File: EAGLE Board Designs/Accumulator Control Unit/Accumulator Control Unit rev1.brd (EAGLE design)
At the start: 186.7 x 135.7 mm, 223 parts, among them J1 CONNECTOR-CAN_MF_T_V_, J2 CONNECTOR-8_MF_T_V_, J3 CONNECTOR-8_MF_T_V_, J4 CONNECTOR-2_MF_T_V_, J5 CONNECTOR-12_MF_T_V_, J6 CONNECTOR-14_MF_T_V_, Q1 TRANSISTOR_N_MOS__PMV15ENEA, Q2 TRANSISTOR_N_MOS__PMV15ENEA, T1 TRANSFORMER_HM2112ZNLT_AIRGAP, U1 RELAY_SOLIDSTATE_NO, U10 OPAMP_1_CHANNEL_OPA991, U11 LOGICGATE_AND_DCK3, U12 OPAMP_1_CHANNEL_OPA991, U13 OPAMP_1_CHANNEL_OPA991, U14 OPAMP_1_CHANNEL_OPA991, U15 LOGICGATE_AND_DCK3, U16 RELAY_SOLIDSTATE_NO, U17 VOLTAGE_REGULATOR_SOT223_3.3V, U18 OPAMP_1_CHANNEL_OPA991, U19 MAX7404, U2 ADG1423, U20 OPAMP_1_CHANNEL_OPA991, U22 OPAMP_1_CHANNEL_OPA991, U25 TCAN1051HQV-Q1, U26 MAX7404, U27 OPAMP_1_CHANNEL_OPA991, U28 MAX7404, U29 OPAMP_1_CHANNEL_OPA991, U3 LM555, U30 MAX7404, U4 OPAMP_1_CHANNEL_OPA991, U5 LTC6820, U6 ADM823, U7 OPAMP_1_CHANNEL_OPA991, U8 LOGICGATE_AND_DCK3, U9 OPAMP_1_CHANNEL_OPA991

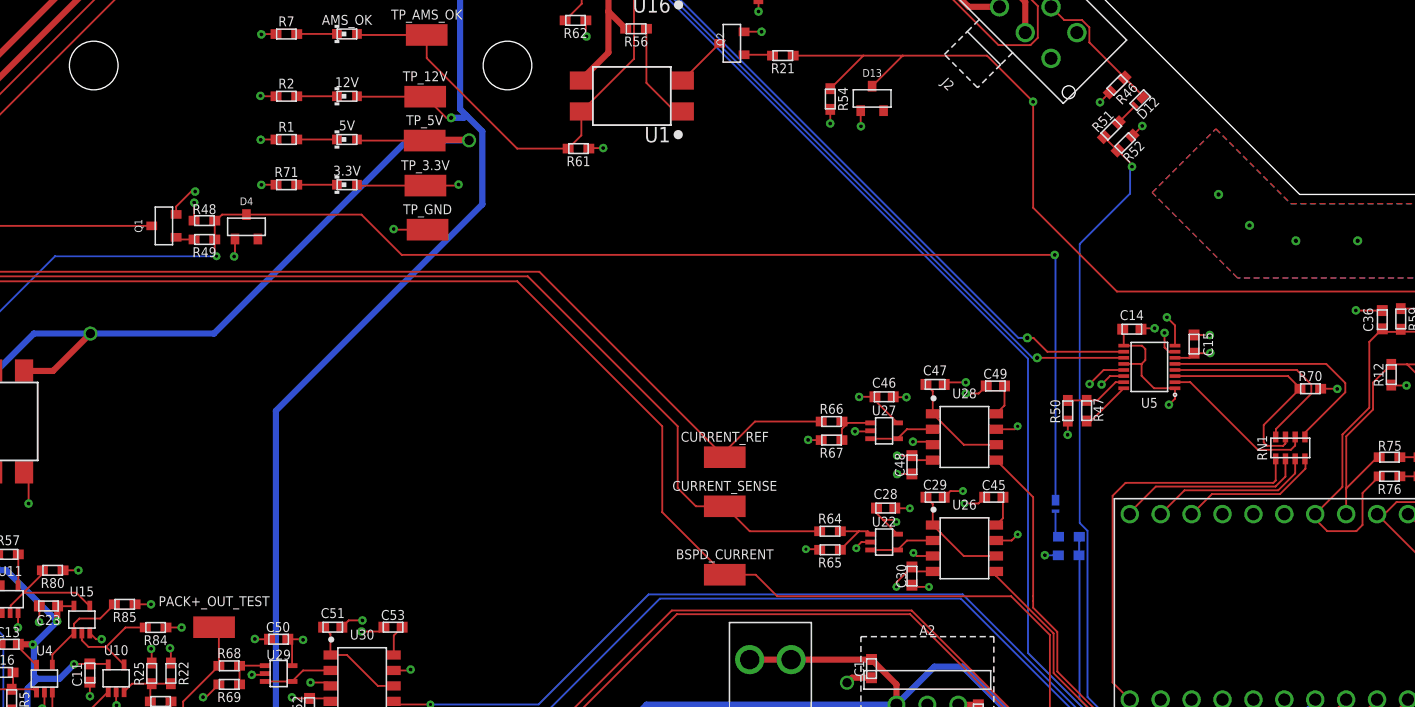
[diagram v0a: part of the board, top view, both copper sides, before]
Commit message: fix miso pullup
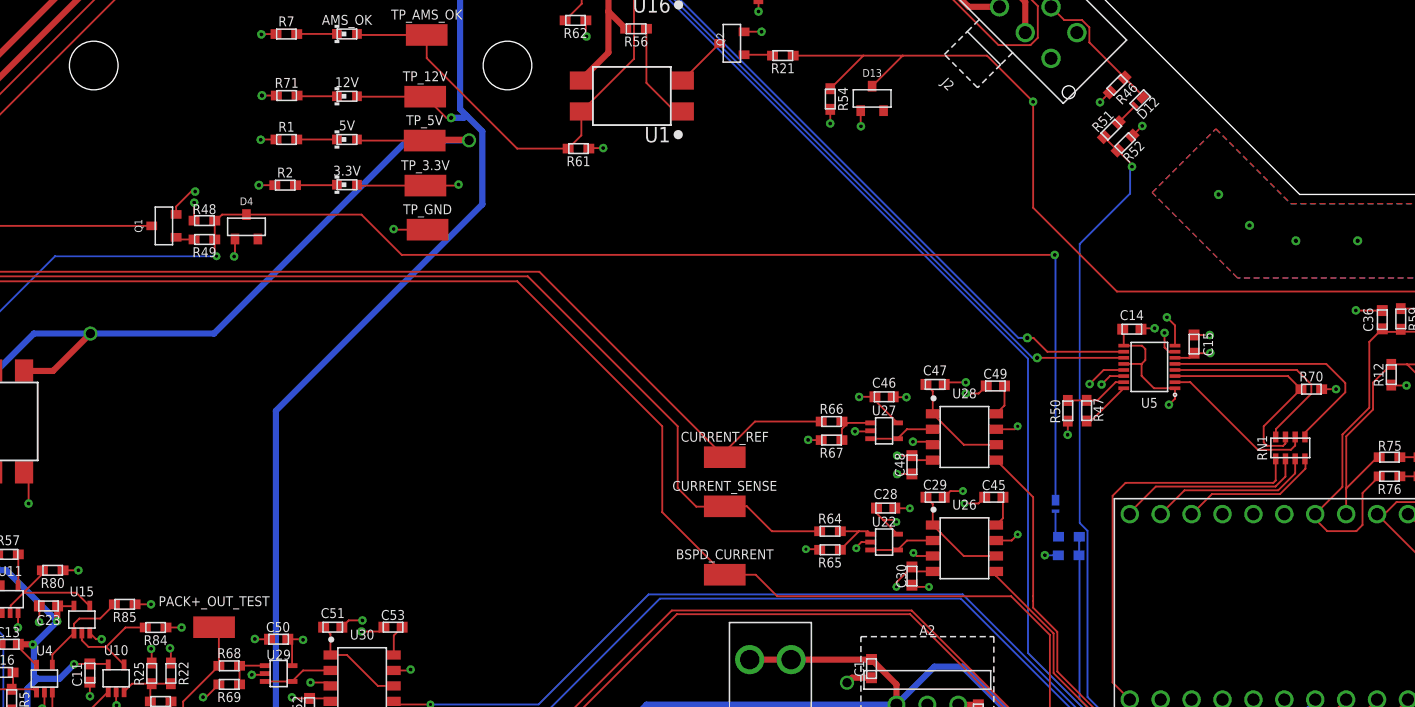
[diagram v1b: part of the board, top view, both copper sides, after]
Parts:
- R2: value RESISTOR_0603_2K -> RESISTOR_0603_1K
- R70: value RESISTOR_0603_10K -> RESISTOR_0603_1K
- R71: value RESISTOR_0603_470 -> RESISTOR_0603_1K; device HyTechDevices - Copy:0603-RES -> HyTechDevices:0603-RES
- moved R71 7.33 mm to (73.3, 80.5)
- moved R2 7.31 mm to (73.2, 73.2)
- moved R70 0.09 mm to (157.5, 56.4)
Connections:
- net N$1: now also R2.2; no longer R71.2
- net N$14: now also R71.2; no longer R2.2

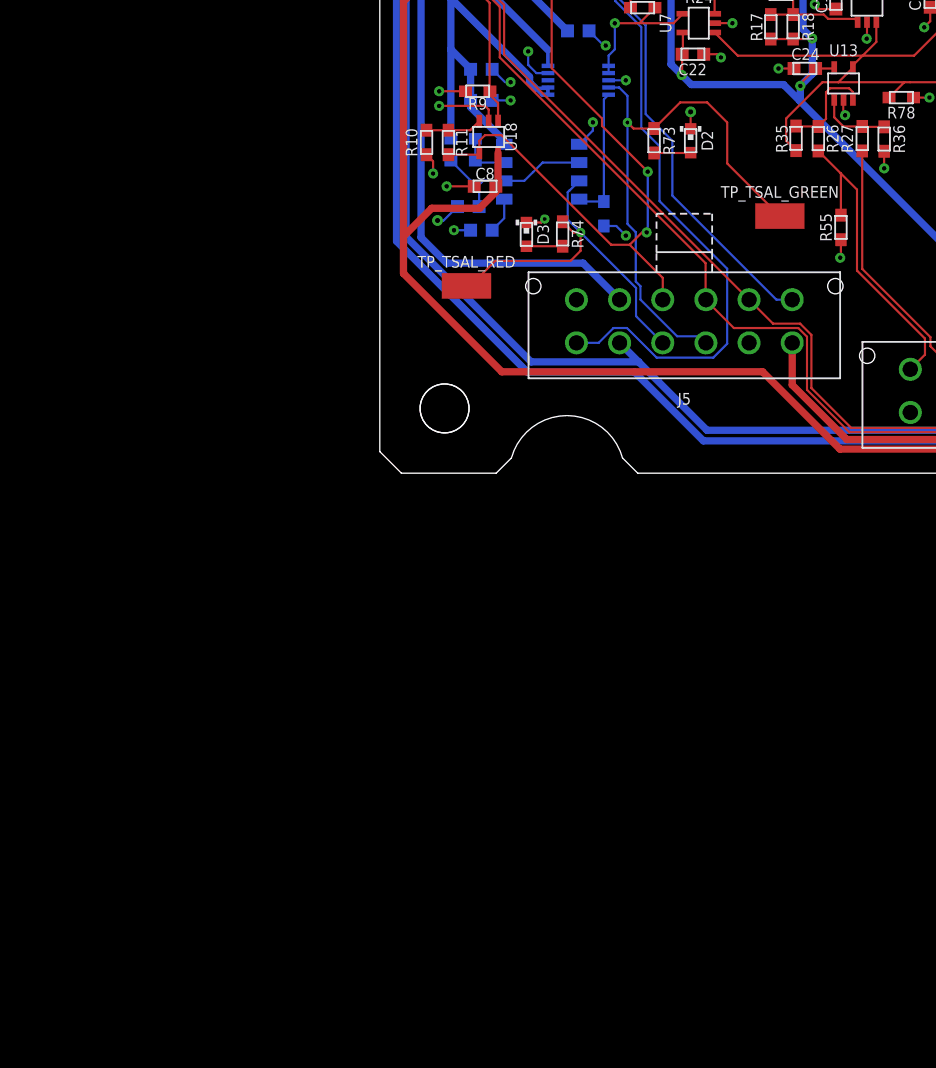
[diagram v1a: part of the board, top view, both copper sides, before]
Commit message: low side switch tsal lights
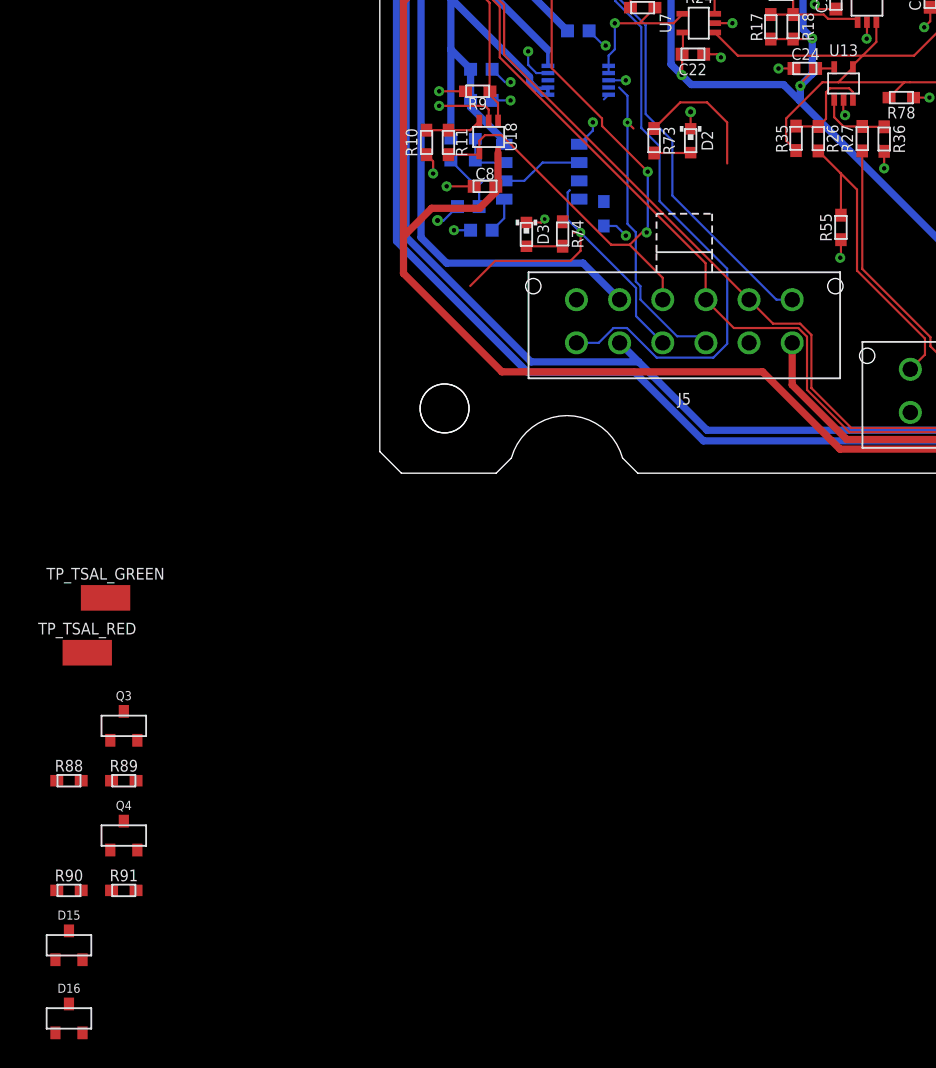
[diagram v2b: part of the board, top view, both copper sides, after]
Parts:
- added D15, D16: TVS_15V, HyTechDevices:SOT-23
- added Q3, Q4: TRANSISTOR_N_MOS__PMV15ENEA, HyTechDevices:SOT-23
- added R88, R90: RESISTOR_0603_10, HyTechDevices:0603-RES
- added R89, R91: RESISTOR_0603_10K, HyTechDevices:0603-RES
- moved TP_TSAL_GREEN 53.8 mm to (-19.1, -10.2)
- moved TP_TSAL_RED 36.6 mm to (-20.3, -14.0)
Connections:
- new net N$60: Q3.1, R88.2
- new net N$61: Q4.1, R90.2
- new net TSAL_GREEN1: D15.3, R90.1, R91.1, TP_TSAL_GREEN.1, U2.9
- new net TSAL_RED1: D16.3, R88.1, R89.1, TP_TSAL_RED.1, U3.3
- net +12V: now also R73.1, R74.1
- net GND: now also D15.1, D16.1, Q3.2, Q4.2, R89.2, R91.2; no longer D2.1, D3.1
- net TSAL_GREEN: now also D2.1, Q4.3; no longer R73.1, TP_TSAL_GREEN.1, U2.9
- net TSAL_RED: now also D3.1, Q3.3; no longer R74.1, TP_TSAL_RED.1, U3.3
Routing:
- net TSAL_GREEN: track 38.3 -> 22.9 mm, vias 1 -> 2
- net +12V: track 583.5 -> 592.7 mm
- net TIMER_EN: track 9.34 -> 0.70 mm
- net GND: track 208.2 -> 205.6 mm, vias 157 -> 155
- net TSAL_RED: track 26.1 -> 25.2 mm, vias 1 -> 2

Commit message: change names of revs
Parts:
- removed D15, D16: TVS_15V, HyTechDevices:SOT-23
- removed Q3, Q4: TRANSISTOR_N_MOS__PMV15ENEA, HyTechDevices:SOT-23
- removed R88, R90: RESISTOR_0603_10, HyTechDevices:0603-RES
- removed R89, R91: RESISTOR_0603_10K, HyTechDevices:0603-RES
- moved TP_TSAL_GREEN 53.8 mm to (27.8, 16.4)
- moved TP_TSAL_RED 36.6 mm to (6.02, 11.5)
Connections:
- removed net N$60: Q3.1, R88.2
- removed net N$61: Q4.1, R90.2
- removed net TSAL_GREEN1: D15.3, R90.1, R91.1, TP_TSAL_GREEN.1, U2.9
- removed net TSAL_RED1: D16.3, R88.1, R89.1, TP_TSAL_RED.1, U3.3
- net +12V: no longer R73.1, R74.1
- net GND: now also D2.1, D3.1; no longer D15.1, D16.1, Q3.2, Q4.2, R89.2, R91.2
- net TSAL_GREEN: now also R73.1, TP_TSAL_GREEN.1, U2.9; no longer D2.1, Q4.3
- net TSAL_RED: now also R74.1, TP_TSAL_RED.1, U3.3; no longer D3.1, Q3.3
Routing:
- net TSAL_GREEN: track 22.9 -> 38.3 mm, vias 2 -> 1
- net +12V: track 592.7 -> 583.5 mm
- net TIMER_EN: track 0.70 -> 9.34 mm
- net GND: track 205.6 -> 208.2 mm, vias 155 -> 157
- net TSAL_RED: track 25.2 -> 26.1 mm, vias 2 -> 1
